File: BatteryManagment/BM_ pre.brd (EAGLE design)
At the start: 160 x 100 mm, 2 parts, among them U1 ATMEGA328P-AU

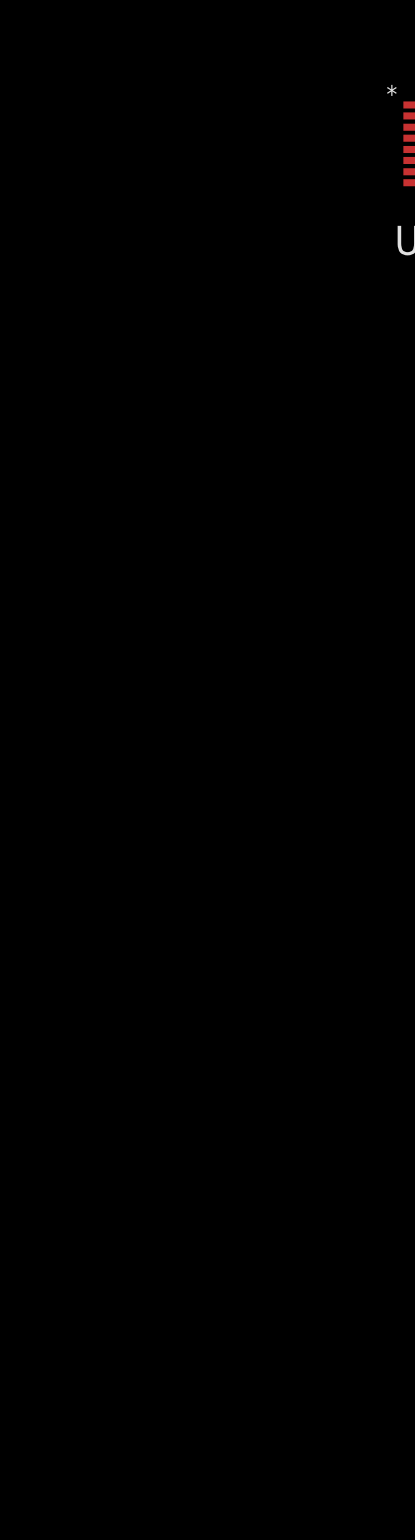
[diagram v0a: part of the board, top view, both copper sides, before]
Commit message: Add 3.3V Step-Down Converter
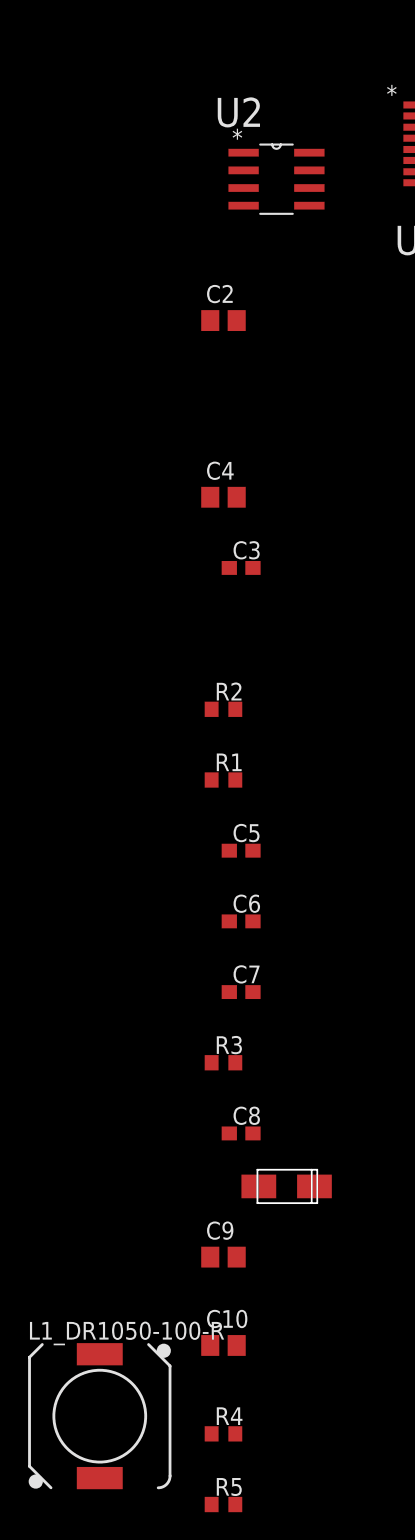
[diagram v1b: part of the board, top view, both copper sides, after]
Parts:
- added C10, C2, C4, C9: 47u, rcl:C0805
- added C3: 10n, rcl:C0603
- added C5: 15n, rcl:C0603
- added C6: 1n, rcl:C0603
- added C7: 47p, rcl:C0603
- added C8: 100n, rcl:C0603
- added L1_DR1050-100-R: 10u, inductors:DR1030
- added R1: 330k, rcl:R0603
- added R2: 68k, rcl:R0603
- added R3: 29.4k, rcl:R0603
- added R4: 10.2k, rcl:R0603
- added R5: 3.24k, rcl:R0603
- added U$1: B240A, BM_pre:B240A
- added U2: TPS54231DR, BM_pre:SOIC127P600X175-8N
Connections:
- removed net N$1: C1.1, U1.18, U1.4, U1.6
- new net +3V3: C1.1, C10.1, C9.1, L1_DR1050-100-R.2, R4.2, U1.18, U1.4, U1.6
- new net N$14: C8.2, L1_DR1050-100-R.1, U$1.P$2, U2.8
- new net N$3: R1.1, R2.2, U2.3
- new net N$4: C5.1, U2.4
- new net N$5: C6.1, C7.1, U2.6
- new net N$7: C6.2, R3.2
- new net N$8: C8.1, U2.1
- new net V+: C2.1, C3.1, C4.1, R1.2, U2.2
- new net VREF_3V3: R4.1, R5.2, U2.5
- net GND: now also C10.2, C2.2, C3.2, C4.2, C5.2, C7.2, C9.2, R2.1, R3.1, R5.1, U$1.P$1, U2.7
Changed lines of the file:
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@@
 <attribute name="SUPPLIER" value="Atmel" x="-33.02" y="8.89" size="1.778" layer="27" display="off"/>
 </element>
+<element name="U2" library="BM_pre" package="SOIC127P600X175-8N" value="TPS54231DR" x="-46.99" y="6.35">
+<attribute name="MPN" value="TPS54231DR" x="-46.99" y="6.35" size="1.778" layer="27" display="off"/>
+<attribute name="OC_FARNELL" value="2120467" x="-46.99" y="6.35" size="1.778" layer="27" display="off"/>
+<attribute name="OC_NEWARK" value="94T5096" x="-46.99" y="6.35" size="1.778" layer="27" display="off"/>
+<attribute name="PACKAGE" value="SOIC- 8" x="-46.99" y="6.35" size="1.778" layer="27" display="off"/>
+<attribute name="SUPPLIER" value="TEXAS INSTRUMENTS" x="-46.99" y="6.35" size="1.778" layer="27" display="off"/>
+</element>
+<element name="C2" library="rcl" package="C0805" value="47u" x="-50.8" y="-3.81"/>
+<element name="C4" library="rcl" package="C0805" value="47u" x="-50.8" y="-16.51"/>
+<element name="C3" library="rcl" package="C0603" value="10n" x="-49.53" y="-21.59"/>
+<element name="R2" library="rcl" package="R0603" value="68k" x="-50.8" y="-31.75"/>
+<element name="R1" library="rcl" package="R0603" value="330k" x="-50.8" y="-36.83"/>
+<element name="C5" library="rcl" package="C0603" value="15n" x="-49.53" y="-41.91"/>
+<element name="C6" library="rcl" package="C0603" value="1n" x="-49.53" y="-46.99"/>
+<element name="C7" library="rcl" package="C0603" value="47p" x="-49.53" y="-52.07"/>
+<element name="R3" library="rcl" package="R0603" value="29.4k" x="-50.8" y="-57.15"/>
+<element name="C8" library="rcl" package="C0603" value="100n" x="-49.53" y="-62.23"/>
+<element name="U$1" library="BM_pre" package="B240A" value="B240A" x="-48.26" y="-66.04"/>
+<element name="C9" library="rcl" package="C0805" value="47u" x="-50.8" y="-71.12"/>
+<element name="C10" library="rcl" package="C0805" value="47u" x="-50.8" y="-77.47"/>
+<element name="R4" library="rcl" package="R0603" value="10.2k" x="-50.8" y="-83.82"/>
+<element name="R5" library="rcl" package="R0603" value="3.24k" x="-50.8" y="-88.9"/>
+<element name="L1_DR1050-100-R" library="inductors" package="DR1030" value="10u" x="-59.69" y="-82.55"/>
 </elements>
 <signals>
-<signal name="N$1">
-<contactref element="U1" pad="4"/>
-<contactref element="C1" pad="1"/>
-<contactref element="U1" pad="18"/>
-<contactref element="U1" pad="6"/>
-<wire x1="-37.1348" y1="7.6962" x2="-37.1348" y2="9.2964" width="0" layer="19" extent="1-1"/>
-<wire x1="-28.9052" y1="6.8834" x2="-37.1348" y2="7.6962" width="0" layer="19" extent="1-1"/>
-<wire x1="-16.09" y1="21.59" x2="-28.9052" y2="6.8834" width="0" layer="19" extent="1-1"/>
-</signal>
 <signal name="GND">
 <contactref element="C1" pad="2"/>
@@
 <contactref element="U1" pad="5"/>
 <contactref element="U1" pad="21"/>
-<wire x1="-37.1348" y1="8.4836" x2="-37.1348" y2="10.0838" width="0" layer="19" extent="1-1"/>
+<contactref element="U2" pad="7"/>
+<contactref element="C4" pad="2"/>
+<contactref element="C2" pad="2"/>
+<contactref element="C3" pad="2"/>
+<contactref element="R2" pad="1"/>
+<contactref element="C5" pad="2"/>
+<contactref element="C10" pad="2"/>
+<contactref element="C9" pad="2"/>
+<contactref element="C7" pad="2"/>
+<contactref element="R3" pad="1"/>
+<contactref element="U$1" pad="P$1"/>
+<contactref element="R5" pad="1"/>
+<wire x1="-49.85" y1="-77.47" x2="-51.65" y2="-88.9" width="0" layer="19" extent="1-1"/>
+<wire x1="-49.85" y1="-71.12" x2="-49.85" y2="-77.47" width="0" layer="19" extent="1-1"/>
+<wire x1="-48.26" y1="-66.04" x2="-49.85" y2="-71.12" width="0" layer="19" extent="1-1"/>
+<wire x1="-51.65" y1="-57.15" x2="-48.26" y2="-66.04" width="0" layer="19" extent="1-1"/>
+<wire x1="-48.68" y1="-52.07" x2="-51.65" y2="-57.15" width="0" layer="19" extent="1-1"/>
+<wire x1="-48.68" y1="-41.91" x2="-48.68" y2="-52.07" width="0" layer="19" extent="1-1"/>
+<wire x1="-51.65" y1="-31.75" x2="-48.68" y2="-41.91" width="0" layer="19" extent="1-1"/>
+<wire x1="-48.68" y1="-21.59" x2="-51.65" y2="-31.75" width="0" layer="19" extent="1-1"/>
+<wire x1="-49.85" y1="-16.51" x2="-48.68" y2="-21.59" width="0" layer="19" extent="1-1"/>
+<wire x1="-49.85" y1="-3.81" x2="-49.85" y2="-16.51" width="0" layer="19" extent="1-1"/>
+<wire x1="-44.6278" y1="6.985" x2="-49.85" y2="-3.81" width="0" layer="19" extent="1-1"/>
+<wire x1="-37.1348" y1="8.4836" x2="-44.6278" y2="6.985" width="0" layer="19" extent="1-1"/>
+<wire x1="-37.1348" y1="10.0838" x2="-37.1348" y2="8.4836" width="0" layer="19" extent="1-1"/>
 <wire x1="-28.9052" y1="9.2964" x2="-37.1348" y2="10.0838" width="0" layer="19" extent="1-1"/>
 <wire x1="-14.39" y1="21.59" x2="-28.9052" y2="9.2964" width="0" layer="19" extent="1-1"/>
 </signal>
+<signal name="N$3">
+<contactref element="U2" pad="3"/>
+<contactref element="R2" pad="2"/>
+<contactref element="R1" pad="1"/>
+<wire x1="-49.95" y1="-31.75" x2="-51.65" y2="-36.83" width="0" layer="19" extent="1-1"/>
+<wire x1="-49.3522" y1="5.715" x2="-49.95" y2="-31.75" width="0" layer="19" extent="1-1"/>
+</signal>
+<signal name="N$4">
+<contactref element="U2" pad="4"/>
+<contactref element="C5" pad="1"/>
+<wire x1="-49.3522" y1="4.445" x2="-50.38" y2="-41.91" width="0" layer="19" extent="1-1"/>
+</signal>
+<signal name="N$5">
+<contactref element="U2" pad="6"/>
+<contactref element="C6" pad="1"/>
+<contactref element="C7" pad="1"/>
+<wire x1="-50.38" y1="-46.99" x2="-50.38" y2="-52.07" width="0" layer="19" extent="1-1"/>
+<wire x1="-44.6278" y1="5.715" x2="-50.38" y2="-46.99" width="0" layer="19" extent="1-1"/>
+</signal>
+<signal name="N$7">
+<contactref element="C6" pad="2"/>
+<contactref element="R3" pad="2"/>
+<wire x1="-48.68" y1="-46.99" x2="-49.95" y2="-57.15" width="0" layer="19" extent="1-1"/>
+</signal>
+<signal name="N$8">
+<contactref element="C8" pad="1"/>
+<contactref element="U2" pad="1"/>
+<wire x1="-49.3522" y1="8.255" x2="-50.38" y2="-62.23" width="0" layer="19" extent="1-1"/>
+</signal>
+<signal name="+3V3">
+<contactref element="C9" pad="1"/>
+<contactref element="C10" pad="1"/>
+<contactref element="R4" pad="2"/>
+<contactref element="L1_DR1050-100-R" pad="2"/>
+<contactref element="C1" pad="1"/>
+<contactref element="U1" pad="4"/>
+<contactref element="U1" pad="18"/>
+<contactref element="U1" pad="6"/>
+<wire x1="-49.95" y1="-83.82" x2="-59.69" y2="-87" width="0" layer="19" extent="1-1"/>
+<wire x1="-51.75" y1="-77.47" x2="-49.95" y2="-83.82" width="0" layer="19" extent="1-1"/>
+<wire x1="-51.75" y1="-71.12" x2="-51.75" y2="-77.47" width="0" layer="19" extent="1-1"/>
+<wire x1="-37.1348" y1="7.6962" x2="-51.75" y2="-71.12" width="0" layer="19" extent="1-1"/>
+<wire x1="-37.1348" y1="9.2964" x2="-37.1348" y2="7.6962" width="0" layer="19" extent="1-1"/>
+<wire x1="-28.9052" y1="6.8834" x2="-37.1348" y2="7.6962" width="0" layer="19" extent="1-1"/>
+<wire x1="-16.09" y1="21.59" x2="-28.9052" y2="6.8834" width="0" layer="19" extent="1-1"/>
+</signal>
+<signal name="N$14">
+<contactref element="U2" pad="8"/>
+<contactref element="C8" pad="2"/>
+<contactref element="U$1" pad="P$2"/>
+<contactref element="L1_DR1050-100-R" pad="1"/>
+<wire x1="-48.68" y1="-62.23" x2="-59.69" y2="-78.1" width="0" layer="19" extent="1-1"/>
+<wire x1="-44.26" y1="-66.04" x2="-48.68" y2="-62.23" width="0" layer="19" extent="1-1"/>
+<wire x1="-44.6278" y1="8.255" x2="-48.68" y2="-62.23" width="0" layer="19" extent="1-1"/>
+</signal>
+<signal name="V+">
+<contactref element="U2" pad="2"/>
+<contactref element="C4" pad="1"/>
+<contactref element="C2" pad="1"/>
+<contactref element="C3" pad="1"/>
+<contactref element="R1" pad="2"/>
+<wire x1="-50.38" y1="-21.59" x2="-49.95" y2="-36.83" width="0" layer="19" extent="1-1"/>
+<wire x1="-51.75" y1="-16.51" x2="-50.38" y2="-21.59" width="0" layer="19" extent="1-1"/>
+<wire x1="-51.75" y1="-3.81" x2="-51.75" y2="-16.51" width="0" layer="19" extent="1-1"/>
+<wire x1="-49.3522" y1="6.985" x2="-51.75" y2="-3.81" width="0" layer="19" extent="1-1"/>
+</signal>
+<signal name="VREF_3V3">
+<contactref element="U2" pad="5"/>
+<contactref element="R4" pad="1"/>
+<contactref element="R5" pad="2"/>
+<wire x1="-51.65" y1="-83.82" x2="-49.95" y2="-88.9" width="0" layer="19" extent="1-1"/>
+<wire x1="-44.6278" y1="4.445" x2="-51.65" y2="-83.82" width="0" layer="19" extent="1-1"/>
+</signal>
 </signals>

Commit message: Library update / Schematic 5V Buck Converter Delete
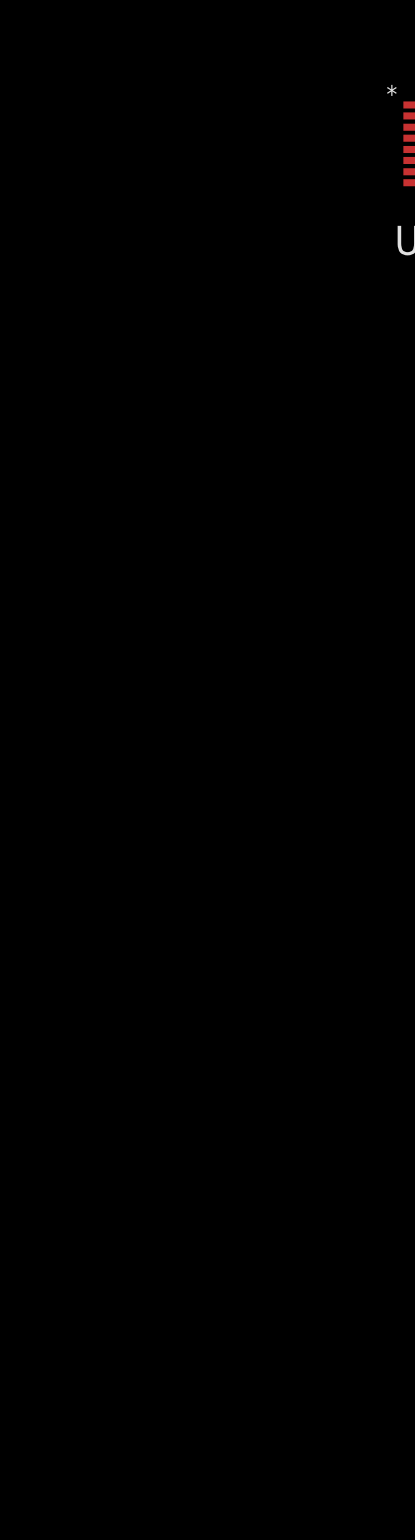
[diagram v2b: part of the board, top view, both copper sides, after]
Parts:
- removed C10, C2, C4, C9: 47u, rcl:C0805
- removed C3: 10n, rcl:C0603
- removed C5: 15n, rcl:C0603
- removed C6: 1n, rcl:C0603
- removed C7: 47p, rcl:C0603
- removed C8: 100n, rcl:C0603
- removed L1_DR1050-100-R: 10u, inductors:DR1030
- removed R1: 330k, rcl:R0603
- removed R2: 68k, rcl:R0603
- removed R3: 29.4k, rcl:R0603
- removed R4: 10.2k, rcl:R0603
- removed R5: 3.24k, rcl:R0603
- removed U$1: B240A, BM_pre:B240A
- removed U2: TPS54231DR, BM_pre:SOIC127P600X175-8N
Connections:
- removed net N$14: C8.2, L1_DR1050-100-R.1, U$1.P$2, U2.8
- removed net N$3: R1.1, R2.2, U2.3
- removed net N$4: C5.1, U2.4
- removed net N$5: C6.1, C7.1, U2.6
- removed net N$7: C6.2, R3.2
- removed net N$8: C8.1, U2.1
- removed net V+: C2.1, C3.1, C4.1, R1.2, U2.2
- removed net VREF_3V3: R4.1, R5.2, U2.5
- net +3V3: no longer C10.1, C9.1, L1_DR1050-100-R.2, R4.2
- net GND: no longer C10.2, C2.2, C3.2, C4.2, C5.2, C7.2, C9.2, R2.1, R3.1, R5.1, U$1.P$1, U2.7
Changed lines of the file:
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@@
 <?xml version="1.0" encoding="utf-8"?>
 <!DOCTYPE eagle SYSTEM "eagle.dtd">
-<eagle version="8.0.2">
+<eagle version="8.1.0">
 <drawing>
 <settings>
@@
 <attribute name="SUPPLIER" value="Atmel" x="-33.02" y="8.89" size="1.778" layer="27" display="off"/>
 </element>
-<element name="U2" library="BM_pre" package="SOIC127P600X175-8N" value="TPS54231DR" x="-46.99" y="6.35">
-<attribute name="MPN" value="TPS54231DR" x="-46.99" y="6.35" size="1.778" layer="27" display="off"/>
-<attribute name="OC_FARNELL" value="2120467" x="-46.99" y="6.35" size="1.778" layer="27" display="off"/>
-<attribute name="OC_NEWARK" value="94T5096" x="-46.99" y="6.35" size="1.778" layer="27" display="off"/>
-<attribute name="PACKAGE" value="SOIC- 8" x="-46.99" y="6.35" size="1.778" layer="27" display="off"/>
-<attribute name="SUPPLIER" value="TEXAS INSTRUMENTS" x="-46.99" y="6.35" size="1.778" layer="27" display="off"/>
-</element>
-<element name="C2" library="rcl" package="C0805" value="47u" x="-50.8" y="-3.81"/>
-<element name="C4" library="rcl" package="C0805" value="47u" x="-50.8" y="-16.51"/>
-<element name="C3" library="rcl" package="C0603" value="10n" x="-49.53" y="-21.59"/>
-<element name="R2" library="rcl" package="R0603" value="68k" x="-50.8" y="-31.75"/>
-<element name="R1" library="rcl" package="R0603" value="330k" x="-50.8" y="-36.83"/>
-<element name="C5" library="rcl" package="C0603" value="15n" x="-49.53" y="-41.91"/>
-<element name="C6" library="rcl" package="C0603" value="1n" x="-49.53" y="-46.99"/>
-<element name="C7" library="rcl" package="C0603" value="47p" x="-49.53" y="-52.07"/>
-<element name="R3" library="rcl" package="R0603" value="29.4k" x="-50.8" y="-57.15"/>
-<element name="C8" library="rcl" package="C0603" value="100n" x="-49.53" y="-62.23"/>
-<element name="U$1" library="BM_pre" package="B240A" value="B240A" x="-48.26" y="-66.04"/>
-<element name="C9" library="rcl" package="C0805" value="47u" x="-50.8" y="-71.12"/>
-<element name="C10" library="rcl" package="C0805" value="47u" x="-50.8" y="-77.47"/>
-<element name="R4" library="rcl" package="R0603" value="10.2k" x="-50.8" y="-83.82"/>
-<element name="R5" library="rcl" package="R0603" value="3.24k" x="-50.8" y="-88.9"/>
-<element name="L1_DR1050-100-R" library="inductors" package="DR1030" value="10u" x="-59.69" y="-82.55"/>
 </elements>
 <signals>
@@
 <contactref element="U1" pad="5"/>
 <contactref element="U1" pad="21"/>
-<contactref element="U2" pad="7"/>
-<contactref element="C4" pad="2"/>
-<contactref element="C2" pad="2"/>
-<contactref element="C3" pad="2"/>
-<contactref element="R2" pad="1"/>
-<contactref element="C5" pad="2"/>
-<contactref element="C10" pad="2"/>
-<contactref element="C9" pad="2"/>
-<contactref element="C7" pad="2"/>
-<contactref element="R3" pad="1"/>
-<contactref element="U$1" pad="P$1"/>
-<contactref element="R5" pad="1"/>
-<wire x1="-49.85" y1="-77.47" x2="-51.65" y2="-88.9" width="0" layer="19" extent="1-1"/>
-<wire x1="-49.85" y1="-71.12" x2="-49.85" y2="-77.47" width="0" layer="19" extent="1-1"/>
-<wire x1="-48.26" y1="-66.04" x2="-49.85" y2="-71.12" width="0" layer="19" extent="1-1"/>
-<wire x1="-51.65" y1="-57.15" x2="-48.26" y2="-66.04" width="0" layer="19" extent="1-1"/>
-<wire x1="-48.68" y1="-52.07" x2="-51.65" y2="-57.15" width="0" layer="19" extent="1-1"/>
-<wire x1="-48.68" y1="-41.91" x2="-48.68" y2="-52.07" width="0" layer="19" extent="1-1"/>
-<wire x1="-51.65" y1="-31.75" x2="-48.68" y2="-41.91" width="0" layer="19" extent="1-1"/>
-<wire x1="-48.68" y1="-21.59" x2="-51.65" y2="-31.75" width="0" layer="19" extent="1-1"/>
-<wire x1="-49.85" y1="-16.51" x2="-48.68" y2="-21.59" width="0" layer="19" extent="1-1"/>
-<wire x1="-49.85" y1="-3.81" x2="-49.85" y2="-16.51" width="0" layer="19" extent="1-1"/>
-<wire x1="-44.6278" y1="6.985" x2="-49.85" y2="-3.81" width="0" layer="19" extent="1-1"/>
-<wire x1="-37.1348" y1="8.4836" x2="-44.6278" y2="6.985" width="0" layer="19" extent="1-1"/>
-<wire x1="-37.1348" y1="10.0838" x2="-37.1348" y2="8.4836" width="0" layer="19" extent="1-1"/>
+<wire x1="-37.1348" y1="8.4836" x2="-37.1348" y2="10.0838" width="0" layer="19" extent="1-1"/>
 <wire x1="-28.9052" y1="9.2964" x2="-37.1348" y2="10.0838" width="0" layer="19" extent="1-1"/>
 <wire x1="-14.39" y1="21.59" x2="-28.9052" y2="9.2964" width="0" layer="19" extent="1-1"/>
 </signal>
-<signal name="N$3">
-<contactref element="U2" pad="3"/>
-<contactref element="R2" pad="2"/>
-<contactref element="R1" pad="1"/>
-<wire x1="-49.95" y1="-31.75" x2="-51.65" y2="-36.83" width="0" layer="19" extent="1-1"/>
-<wire x1="-49.3522" y1="5.715" x2="-49.95" y2="-31.75" width="0" layer="19" extent="1-1"/>
-</signal>
-<signal name="N$4">
-<contactref element="U2" pad="4"/>
-<contactref element="C5" pad="1"/>
-<wire x1="-49.3522" y1="4.445" x2="-50.38" y2="-41.91" width="0" layer="19" extent="1-1"/>
-</signal>
-<signal name="N$5">
-<contactref element="U2" pad="6"/>
-<contactref element="C6" pad="1"/>
-<contactref element="C7" pad="1"/>
-<wire x1="-50.38" y1="-46.99" x2="-50.38" y2="-52.07" width="0" layer="19" extent="1-1"/>
-<wire x1="-44.6278" y1="5.715" x2="-50.38" y2="-46.99" width="0" layer="19" extent="1-1"/>
-</signal>
-<signal name="N$7">
-<contactref element="C6" pad="2"/>
-<contactref element="R3" pad="2"/>
-<wire x1="-48.68" y1="-46.99" x2="-49.95" y2="-57.15" width="0" layer="19" extent="1-1"/>
-</signal>
-<signal name="N$8">
-<contactref element="C8" pad="1"/>
-<contactref element="U2" pad="1"/>
-<wire x1="-49.3522" y1="8.255" x2="-50.38" y2="-62.23" width="0" layer="19" extent="1-1"/>
-</signal>
 <signal name="+3V3">
-<contactref element="C9" pad="1"/>
-<contactref element="C10" pad="1"/>
-<contactref element="R4" pad="2"/>
-<contactref element="L1_DR1050-100-R" pad="2"/>
 <contactref element="C1" pad="1"/>
 <contactref element="U1" pad="4"/>
 <contactref element="U1" pad="18"/>
 <contactref element="U1" pad="6"/>
-<wire x1="-49.95" y1="-83.82" x2="-59.69" y2="-87" width="0" layer="19" extent="1-1"/>
-<wire x1="-51.75" y1="-77.47" x2="-49.95" y2="-83.82" width="0" layer="19" extent="1-1"/>
-<wire x1="-51.75" y1="-71.12" x2="-51.75" y2="-77.47" width="0" layer="19" extent="1-1"/>
-<wire x1="-37.1348" y1="7.6962" x2="-51.75" y2="-71.12" width="0" layer="19" extent="1-1"/>
-<wire x1="-37.1348" y1="9.2964" x2="-37.1348" y2="7.6962" width="0" layer="19" extent="1-1"/>
+<wire x1="-37.1348" y1="7.6962" x2="-37.1348" y2="9.2964" width="0" layer="19" extent="1-1"/>
 <wire x1="-28.9052" y1="6.8834" x2="-37.1348" y2="7.6962" width="0" layer="19" extent="1-1"/>
 <wire x1="-16.09" y1="21.59" x2="-28.9052" y2="6.8834" width="0" layer="19" extent="1-1"/>
 </signal>
-<signal name="N$14">
-<contactref element="U2" pad="8"/>
-<contactref element="C8" pad="2"/>
-<contactref element="U$1" pad="P$2"/>
-<contactref element="L1_DR1050-100-R" pad="1"/>
-<wire x1="-48.68" y1="-62.23" x2="-59.69" y2="-78.1" width="0" layer="19" extent="1-1"/>
-<wire x1="-44.26" y1="-66.04" x2="-48.68" y2="-62.23" width="0" layer="19" extent="1-1"/>
-<wire x1="-44.6278" y1="8.255" x2="-48.68" y2="-62.23" width="0" layer="19" extent="1-1"/>
-</signal>
-<signal name="V+">
-<contactref element="U2" pad="2"/>
-<contactref element="C4" pad="1"/>
-<contactref element="C2" pad="1"/>
-<contactref element="C3" pad="1"/>
-<contactref element="R1" pad="2"/>
-<wire x1="-50.38" y1="-21.59" x2="-49.95" y2="-36.83" width="0" layer="19" extent="1-1"/>
-<wire x1="-51.75" y1="-16.51" x2="-50.38" y2="-21.59" width="0" layer="19" extent="1-1"/>
-<wire x1="-51.75" y1="-3.81" x2="-51.75" y2="-16.51" width="0" layer="19" extent="1-1"/>
-<wire x1="-49.3522" y1="6.985" x2="-51.75" y2="-3.81" width="0" layer="19" extent="1-1"/>
-</signal>
-<signal name="VREF_3V3">
-<contactref element="U2" pad="5"/>
-<contactref element="R4" pad="1"/>
-<contactref element="R5" pad="2"/>
-<wire x1="-51.65" y1="-83.82" x2="-49.95" y2="-88.9" width="0" layer="19" extent="1-1"/>
-<wire x1="-44.6278" y1="4.445" x2="-51.65" y2="-83.82" width="0" layer="19" extent="1-1"/>
-</signal>
 </signals>
